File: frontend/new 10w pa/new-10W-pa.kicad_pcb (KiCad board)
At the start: 2 copper layers, 100 x 100 mm, 177 parts, among them K1 D3002, K2 D3002, K3 D3002, K4 D3002, K5 D3002, K6 D3002, P1 CONN_01X02, P2 CONN_02X01, P3 From HL CN3, P4 CONN_01X02, P5 CONN_01X02, P6 CONN_01X01, P7 From FE CN2, P8 CONN_01X07, Q1 2N3906, Q2 2N3906, Q3 RD16HHF1, T1 TRANSFO, T2 TRANSFO, U1 74HC14, U2 74HC14, U3 TPIC6B595, U4 TPIC6B595, U5 TPIC6B595, U6 TPIC6B595

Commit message: Starting Layout
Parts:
- removed R9: Microstrip, Resistors_SMD:R_0805
- added C78: 150pF, Capacitors_SMD:C_0805, F.Cu at (131.5, 112.3)
- added C79: 150pF, Capacitors_SMD:C_0805, F.Cu at (124.9, 112.3)
- added P9: CONN_02X05, Pin_Headers:Pin_Header_Straight_2x05, F.Cu at (163.3, 138.9)
- C57, C68: value 300pF -> 150pF
- P8: value CONN_01X07 -> CONN_01X08; footprint Pin_Headers:Pin_Header_Straight_1x07 -> Pin_Headers:Pin_Header_Straight_1x08
- R2, R3, R4: footprint Resistors_SMD:R_0805 -> Resistors_ThroughHole:Resistor_Vertical_RM5mm
- moved R4 107.4 mm to (120.9, 56.0), turned to 90 degrees
- moved C5 107.2 mm to (107.8, 64.4)
- moved R3 102.3 mm to (116.5, 56.5), turned to 270 degrees
- moved R2 98.4 mm to (111.9, 55.8), turned to 90 degrees
- moved R5 97.8 mm to (126.1, 68.3)
- moved C3 97.7 mm to (126.0, 62.9)
- moved C4 95.8 mm to (121.3, 62.9)
- moved C6 92.4 mm to (133.6, 62.9)
- moved D7 91.4 mm to (106.6, 147.3)
- moved D8 89.7 mm to (129.3, 147.2)
- moved R10 87.3 mm to (138.5, 60.4)
- moved C1 84.8 mm to (107.7, 70.0), turned to 0 degrees
- moved D14 84.1 mm to (137.0, 147.3)
- moved C51 83.8 mm to (136.7, 142.5)
- moved C9 79.8 mm to (159.3, 55.2)
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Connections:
- L37 pad 1: Net-(C68-Pad1) -> Net-(L37-Pad1)
- P8 pad 6: /PTT -> Net-(P8-Pad6)
- P8 pad 7: GND -> /PTT
- Q3 pad 1: Net-(Q3-Pad1) -> Net-(C6-Pad2)
- U3 pad 17: Net-(U3-Pad17) -> Net-(P8-Pad6)
- U3 pad 4: Net-(U3-Pad4) -> ANT1
- U3 pad 5: Net-(U3-Pad5) -> ANT2
- U3 pad 6: Net-(U3-Pad6) -> ANT3

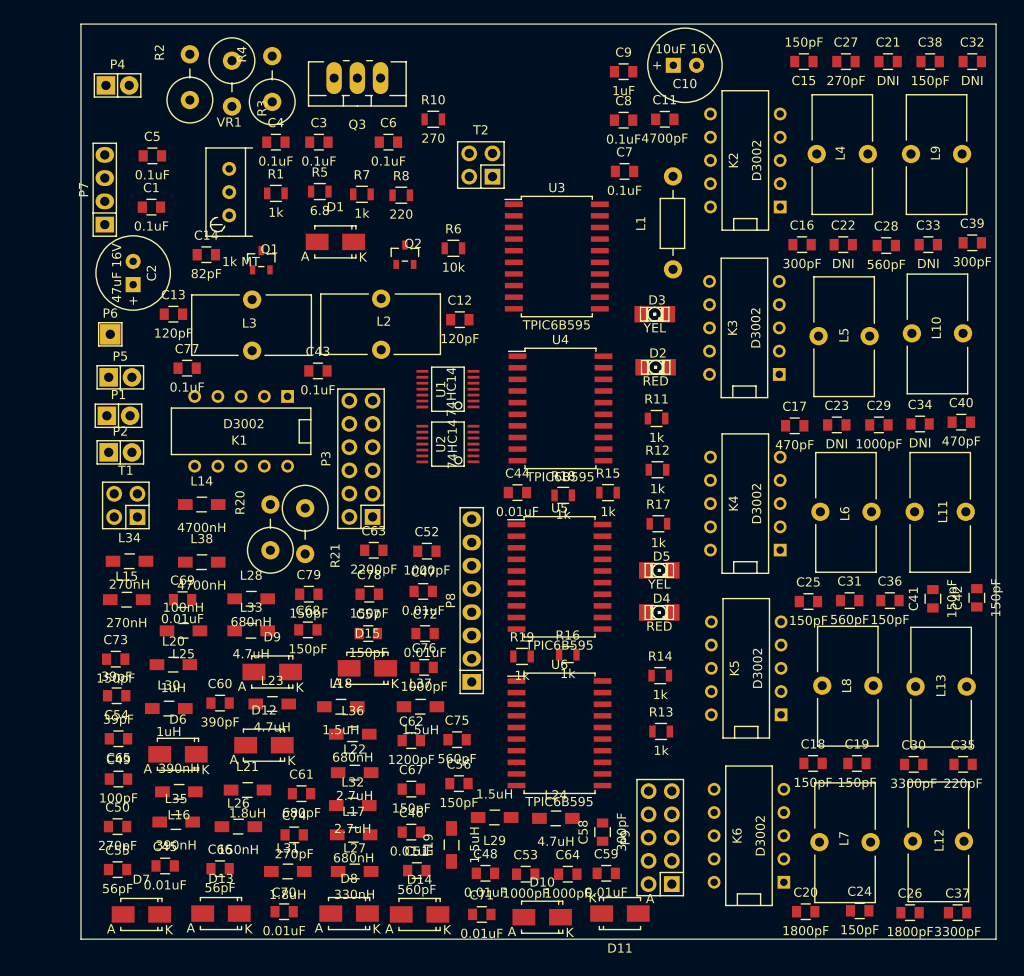
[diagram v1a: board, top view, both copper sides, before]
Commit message: Continuing board routing
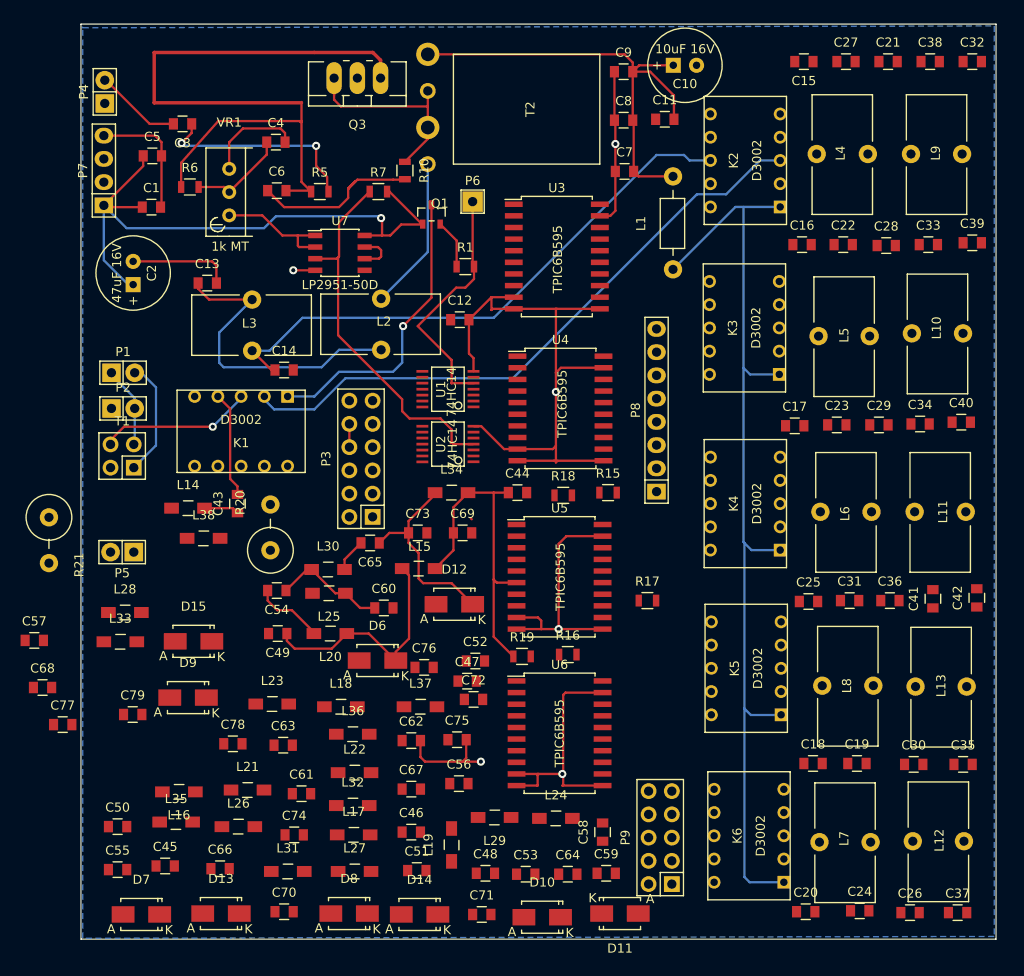
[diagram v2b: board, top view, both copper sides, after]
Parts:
- removed D1: 1N5231, Diodes_SMD:Diode-SMA_Standard
- removed D2, D4: RED, LEDs:LED-1206
- removed D3, D5: YEL, LEDs:LED-1206
- removed Q2: 2N3906, Transistors_SMD:sot23
- removed R11, R12, R13, R14: 1k, Resistors_SMD:R_0805
- removed R2, R4: DNI, Resistors_ThroughHole:Resistor_Vertical_RM5mm
- removed R3: 0, Resistors_ThroughHole:Resistor_Vertical_RM5mm
- removed R8: 220, Resistors_SMD:R_0805
- added U7: LP2951-50D, Housings_SOIC:SOIC-8_3.9x4.9mm_Pitch1.27mm, F.Cu at (128.3, 75.0)
- C1, C11, C12, C13, C14, C15, C16, C17, C18, C19, C20, C21, C22, C23, C24, C25, C26, C27, C28, C29, C3, C30, C31, C32, C33, C34, C35, C36, C37, C38, C39, C4, C40, C41, C42, C43, C44, C45, C46, C47, C48, C49, C5, C50, C51, C52, C53, C54, C55, C56, C57, C58, C59, C6, C60, C61, C62, C63, C64, C65, C66, C67, C68, C69, C7, C70, C71, C72, C73, C74, C75, C76, C77, C78, C79, C8, C9: footprint Capacitors_SMD:C_0805 -> HERMESLITE:C_0805
- K1, K2, K3, K4, K5, K6: footprint Sockets_DIP:DIP-10__300 -> HERMESLITE:D3002
- L14, L15, L16, L17, L18, L19, L20, L21, L22, L23, L24, L25, L26, L27, L28, L29, L30, L31, L32, L33, L34, L35, L36, L37, L38: footprint Choke_SMD:Choke_SMD_1206_Standard -> HERMESLITE:Choke_SMD_1206_Standard
- R1, R10, R15, R16, R17, R18, R19, R5, R6: footprint Resistors_SMD:R_0805 -> HERMESLITE:R_0805
- R7: value 1k -> 10k; footprint Resistors_SMD:R_0805 -> HERMESLITE:R_0805
- T2: value TRANSFO -> OUT_TRANSF; footprint Socket_Strips:Socket_Strip_Straight_2x02 -> HERMESLITE:OUT_TRANSF
- moved P6 42.2 mm to (142.8, 69.4)
- moved C77 41.3 mm to (98.0, 126.5)
- moved C57 36.5 mm to (94.9, 117.3)
- moved L34 36.0 mm to (140.5, 101.2)
- moved C73 35.8 mm to (136.8, 105.6)
- moved C65 34.8 mm to (131.6, 106.7)
- moved L15 32.1 mm to (136.9, 109.5)
- moved C69 31.5 mm to (141.7, 105.6)
- moved C68 29.7 mm to (95.8, 122.5)
- moved R6 29.6 mm to (111.9, 67.8)
- moved P8 29.0 mm to (162.9, 92.2)
- moved R21 28.0 mm to (96.5, 106.4)
- moved D12 25.9 mm to (140.8, 113.4)
- moved D6 24.1 mm to (132.4, 119.5)
- moved C49 23.6 mm to (121.5, 116.6), turned to 180 degrees
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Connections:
- C5 pad 1: Net-(C5-Pad1) -> +12V
- L37 pad 1: Net-(L37-Pad1) -> Net-(C68-Pad1)
- P4 pad 2: Net-(P4-Pad2) -> Net-(C3-Pad2)
- R7 pad 1: Net-(Q2-Pad2) -> /PTT
- R7 pad 2: Net-(P6-Pad1) -> +12V
- T2 pad 3: Net-(C12-Pad1) -> Net-(Q3-Pad3)
- T2 pad 4: Net-(Q3-Pad3) -> Net-(C12-Pad1)
- VR1 pad 1: Net-(C5-Pad1) -> Net-(U7-Pad1)
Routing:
- net GND: track 0.00 -> 192.1 mm, vias 0 -> 6
- net +12V: track 0.00 -> 172.9 mm, vias 0 -> 1
- net Net-(C6-Pad2): track 0.00 -> 79.8 mm
- net TXOUT: track 0.00 -> 68.4 mm
- net TXIN: track 0.00 -> 62.6 mm
- net Net-(C10-Pad1): track 0.00 -> 52.1 mm
- net /PTT: track 0.00 -> 41.1 mm
- net Net-(C44-Pad1): track 0.00 -> 36.1 mm
- net Net-(C13-Pad1): track 0.00 -> 34.1 mm
- net Net-(K1-Pad1): track 0.00 -> 32.6 mm, vias 0 -> 1
- net Net-(P6-Pad1): track 0.00 -> 27.0 mm
- net Net-(C49-Pad1): track 0.00 -> 25.9 mm
- net Net-(Q3-Pad3): track 0.00 -> 23.6 mm
- net Net-(C3-Pad1): track 0.00 -> 23.1 mm, vias 0 -> 2
- net Net-(C65-Pad1): track 0.00 -> 21.8 mm
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- added copper zone on B.Cu, net GND
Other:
- net class Microstrip added: clearance 0.254, trace_width 0.381, via_dia 0.889, via_drill 0.635

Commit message: Continuing routing
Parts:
- added C80: 150pF, HERMESLITE:C_0805, F.Cu at (188.4, 79.7)
- added C81: 150pF, HERMESLITE:C_0805, F.Cu at (188.7, 87.7)
- C16, C39: value 300pF -> 150pF
- moved C37 19.9 mm to (184.5, 130.7), turned to 180 degrees
- moved C18 18.1 mm to (179.8, 112.7), turned to 90 degrees
- moved R18 17.6 mm to (152.4, 119.1)
- moved P9 10.3 mm to (161.9, 128.7)
- moved R15 9.90 mm to (161.6, 110.3)
- moved R16 9.50 mm to (161.7, 114.6)
- moved C28 8.85 mm to (196.8, 73.9)
- moved C20 7.16 mm to (186.4, 147.2)
- moved C34 6.47 mm to (188.7, 99.4), turned to 270 degrees
- moved R17 6.27 mm to (159.8, 118.9)
- moved C19 6.04 mm to (188.9, 126.3), turned to 270 degrees
- moved C36 5.76 mm to (188.8, 118.7), turned to 270 degrees
- moved P8 5.49 mm to (162.8, 97.7), turned to 270 degrees
- moved C33 4.96 mm to (187.6, 74.0)
- moved C15 4.88 mm to (183.9, 54.0)
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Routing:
- net SPI-CLK: track 0.00 -> 103.6 mm, vias 0 -> 2
- net Net-(K6-Pad10): track 0.00 -> 84.9 mm, vias 0 -> 1
- net +5V: track 0.00 -> 75.8 mm, vias 0 -> 4
- net ANT1: track 0.00 -> 72.7 mm, vias 0 -> 2
- net Net-(K5-Pad10): track 0.00 -> 64.7 mm, vias 0 -> 1
- net ANT2: track 0.00 -> 63.1 mm, vias 0 -> 1
- net ANT3: track 0.00 -> 57.8 mm, vias 0 -> 1
- net TX-Load: track 0.00 -> 54.2 mm, vias 0 -> 2
- net Net-(C22-Pad2): track 0.00 -> 52.4 mm
- net Net-(K4-Pad10): track 0.00 -> 51.5 mm, vias 0 -> 1
- net Net-(C30-Pad1): track 0.00 -> 45.2 mm
- net Net-(C35-Pad1): track 0.00 -> 43.0 mm
- net Net-(P8-Pad6): track 0.00 -> 41.9 mm, vias 0 -> 1
- net Net-(C21-Pad2): track 0.00 -> 40.0 mm
- net Net-(C36-Pad2): track 0.00 -> 39.3 mm, vias 0 -> 1
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
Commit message: Plotting complete
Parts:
- added MountingHole_2-7mm: VAL**, Mounting_Holes:MountingHole_2-7mm, F.Cu at (130.2, 63.6)
- moved C63 31.9 mm to (106.2, 101.2), turned to 180 degrees
- moved C52 31.7 mm to (111.5, 117.2)
- moved C78 26.6 mm to (103.3, 105.7)
- moved R21 23.4 mm to (119.9, 107.6), turned to 0 degrees
- moved C77 20.2 mm to (117.2, 120.3)
- moved C71 17.4 mm to (131.4, 135.0), turned to 180 degrees
- moved L23 15.1 mm to (111.5, 112.5)
- moved C67 12.8 mm to (124.4, 128.5)
- moved P5 12.6 mm to (104.1, 120.3)
- moved D10 12.6 mm to (137.9, 146.7)
- moved C47 12.6 mm to (129.9, 124.2)
- moved R20 12.1 mm to (108.9, 107.6), turned to 180 degrees
- moved L32 11.9 mm to (141.2, 132.4), turned to 180 degrees
- moved D11 11.8 mm to (147.1, 146.6), turned to 0 degrees
- moved D15 11.7 mm to (123.7, 119.9)
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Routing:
- net GND: track 190.8 -> 456.1 mm, vias 20 -> 33
- net +12V: track 210.1 -> 338.3 mm, vias 4 -> 10
- net Net-(C77-Pad2): track 0.00 -> 109.2 mm, vias 0 -> 2
- net Net-(C43-Pad1): track 3.81 -> 112.6 mm, vias 0 -> 5
- net Net-(C48-Pad1): track 3.85 -> 88.2 mm, vias 0 -> 2
- net Net-(C45-Pad1): track 13.1 -> 92.9 mm, vias 0 -> 2
- net Net-(C47-Pad1): track 6.26 -> 84.4 mm, vias 0 -> 2
- net +5V: track 75.8 -> 147.3 mm, vias 4 -> 9
- net SPI-DATA: track 0.00 -> 63.6 mm, vias 0 -> 3
- net Net-(C68-Pad1): track 0.00 -> 58.7 mm
- net RX-Load: track 25.6 -> 81.5 mm, vias 0 -> 2
- net Net-(C46-Pad1): track 9.13 -> 58.4 mm, vias 0 -> 4
- net Net-(C67-Pad1): track 0.00 -> 46.7 mm, vias 0 -> 2
- net Net-(C56-Pad1): track 0.00 -> 37.7 mm
- net Net-(C53-Pad1): track 0.00 -> 36.2 mm
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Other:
- board text added: "AC9HY/WA2EUJ PA Ver 1.0"
